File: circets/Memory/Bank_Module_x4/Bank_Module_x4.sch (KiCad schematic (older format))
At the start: 27 parts

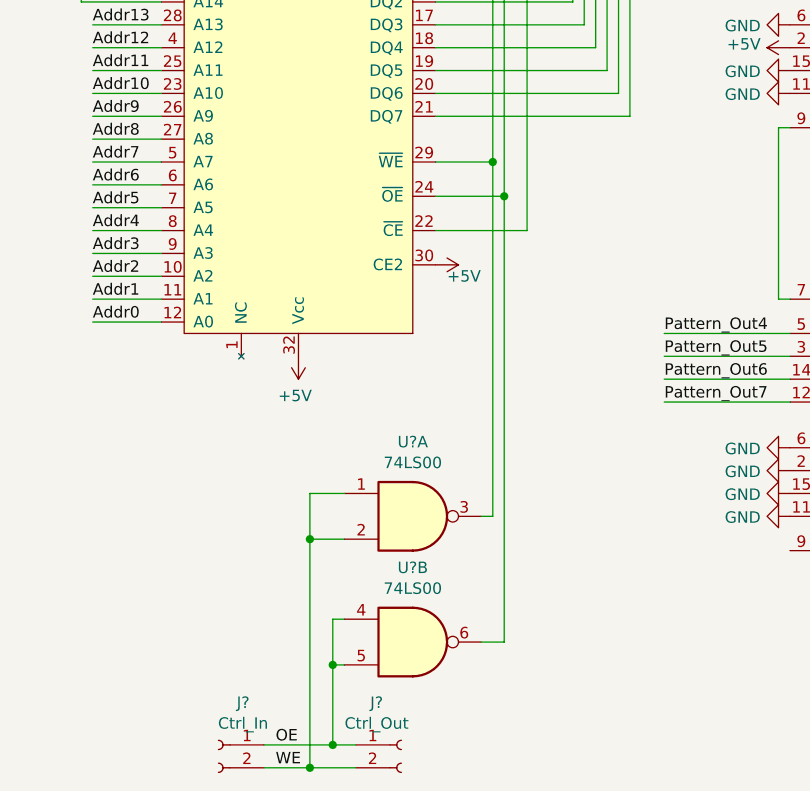
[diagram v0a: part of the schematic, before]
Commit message: Build Schematics for Bank Controller + minor optimaization to eliminat a NAND from Bank Modules
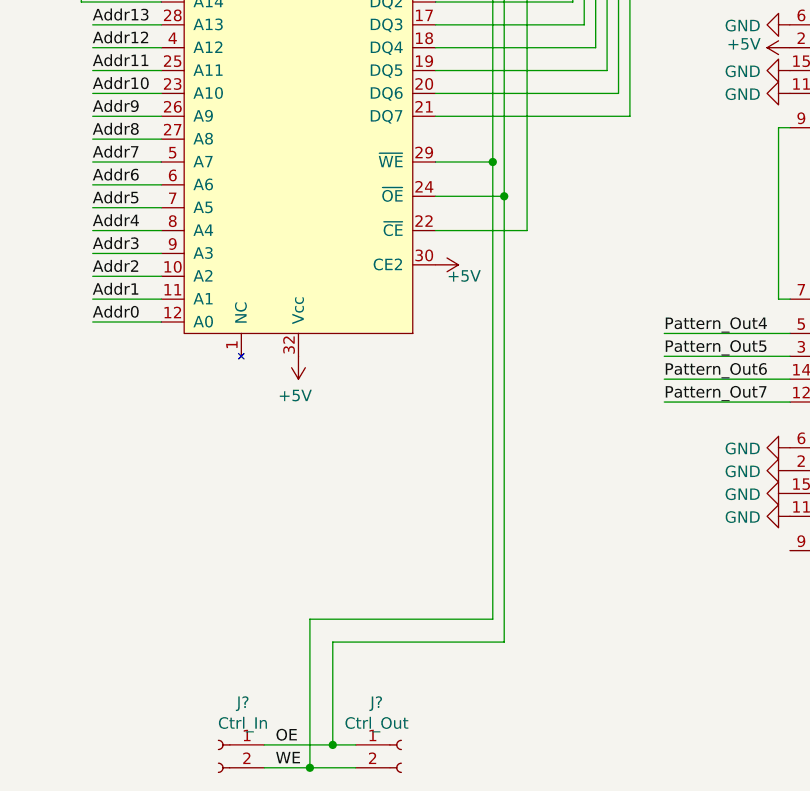
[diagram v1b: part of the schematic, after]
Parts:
- removed U? (x2): 74LS00, symbol 74xx:74LS00
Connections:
- net OE: now also U?.24 (~OE), U?.24 (~OE)
- net WE: now also U?.29 (~WE), U?.29 (~WE)
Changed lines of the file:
@@
 Comment1 ""
 Comment2 "https://github.com/jufo-ufo/Breadboard-Computer/blob/master/LICENSE"
-Comment3 "Apache License 2.0"
+Comment3 "License: Apache License 2.0"
 Comment4 "Author: Alexander Wersching"
 $EndDescr
@@
 	5300 6850 5600 6850
 Connection ~ 5600 6850
-Wire Wire Line
-	6350 6400 6250 6400
-Wire Wire Line
-	6300 5850 6250 5850
-Wire Wire Line
-	5650 5750 5500 5750
-Wire Wire Line
-	5650 6500 5600 6500
-Wire Wire Line
-	5600 6500 5600 6300
-Wire Wire Line
-	5600 6500 5600 6850
-Connection ~ 5600 6500
-Wire Wire Line
-	5500 5750 5500 5950
-Wire Wire Line
-	5500 5950 5500 6950
-Connection ~ 5500 5950
-Wire Wire Line
-	5650 5950 5500 5950
-Wire Wire Line
-	5600 6300 5650 6300
-$Comp
-L 74xx:74LS00 U?
-U 2 1 624E0AB4
-P 5950 6400
-F 0 "U?" H 5950 6725 50  0000 C CNN
-F 1 "74LS00" H 5950 6634 50  0000 C CNN
-F 2 "" H 5950 6400 50  0001 C CNN
-F 3 "http://www.ti.com/lit/gpn/sn74ls00" H 5950 6400 50  0001 C CNN
-	2    5950 6400
-	1    0    0    -1
-$EndComp
-$Comp
-L 74xx:74LS00 U?
-U 1 1 624DFB2D
-P 5950 5850
-F 0 "U?" H 5950 6175 50  0000 C CNN
-F 1 "74LS00" H 5950 6084 50  0000 C CNN
-F 2 "" H 5950 5850 50  0001 C CNN
-F 3 "http://www.ti.com/lit/gpn/sn74ls00" H 5950 5850 50  0001 C CNN
-	1    5950 5850
-	1    0    0    -1
-$EndComp
 $Comp
 L Computer_Component_Library:AS6C1008-55PCN U?
@@
 Connection ~ 6300 4300
 Wire Wire Line
-	6300 4300 6300 5850
+	6300 4300 6300 6300
 Wire Wire Line
 	6350 4450 6050 4450
@@
 Wire Wire Line
 	4250 1900 4150 1900
+Wire Wire Line
+	5600 6400 6350 6400
+Wire Wire Line
+	5600 6400 5600 6850
+Wire Wire Line
+	5500 6300 6300 6300
+Wire Wire Line
+	5500 6300 5500 6950
 $EndSCHEMATC

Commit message: Fixed alot of Issues in Memory Module
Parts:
- removed U?: 74LS86, symbol 74xx:74LS86
- removed U?: 74LS00, symbol 74xx:74LS00
- added U?: 74LS86, symbol 74xx:74LS86
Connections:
- net +5V: now also U?.15 (B3), U?.12; no longer U?.2 (B2)
- net GND: now also U?.2 (B2), U?.3; no longer U?.15 (B3)
- net OE: now also J?.2 (Pin_2), J?.2 (Pin_2); no longer J?.1 (Pin_1), J?.1 (Pin_1)
- net Pattern_In0: now also U?.5 (A1)
- net Pattern_In1: now also U?.3 (A2)
- net Pattern_In2: now also U?.14 (A3)
- net Pattern_In3: now also U?.12 (A4)
- net Pattern_In4: now also U?.5 (A1)
- net Pattern_In5: now also U?.3 (A2)
- net Pattern_In6: now also U?.14 (A3)
- net Pattern_In7: now also U?.12 (A4)
- net Pattern_Out0: no longer U?.5 (A1)
- net Pattern_Out1: no longer U?.3 (A2)
- net Pattern_Out2: no longer U?.14 (A3)
- net Pattern_Out3: no longer U?.12 (A4)
- net Pattern_Out4: no longer U?.5 (A1)
- net Pattern_Out5: no longer U?.3 (A2)
- net Pattern_Out6: no longer U?.14 (A3)
- net Pattern_Out7: no longer U?.12 (A4)
- net WE: now also J?.1 (Pin_1), J?.1 (Pin_1); no longer J?.2 (Pin_2), J?.2 (Pin_2)
- net at U?.22 (~CE), U?.22 (~CE): now also U?.11; no longer U?.13
- new net: U?.13, U?.13
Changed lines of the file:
@@
-$Comp
-L 74xx:74LS86 U?
-U 2 1 61EF8B7A
-P 2350 2850
-F 0 "U?" H 2350 3175 50  0000 C CNN
-F 1 "74LS86" H 2350 3084 50  0000 C CNN
-F 2 "" H 2350 2850 50  0001 C CNN
-F 3 "74xx/74ls86.pdf" H 2350 2850 50  0001 C CNN
-	2    2350 2850
-	1    0    0    -1
-$EndComp
 $Comp
 L 74xx:74LS86 U?
@@
 $EndComp
 Wire Wire Line
-	1500 2750 2050 2750
-Wire Wire Line
 	1450 3300 2050 3300
 Wire Wire Line
@@
 	1350 4400 2050 4400
 Wire Wire Line
-	1500 2300 1500 2750
-Wire Wire Line
 	1450 2400 1450 3300
 Wire Wire Line
@@
 Wire Wire Line
 	1850 3500 1850 1400
-Wire Wire Line
-	2050 2950 1900 2950
-Wire Wire Line
-	1900 2950 1900 1300
-Wire Wire Line
-	2650 2850 2800 2850
-Wire Wire Line
-	2800 2850 2800 1650
 Wire Wire Line
 	2850 1750 2850 3400
@@
 Wire Wire Line
 	3150 1750 2850 1750
-Wire Wire Line
-	2800 1650 3150 1650
 Wire Wire Line
 	3150 2250 3100 2250
@@
 	6050 1600 7000 1600
 $Comp
-L 74xx:74LS00 U?
-U 5 1 624E2056
-P 9500 1650
-F 0 "U?" H 9730 1696 50  0000 L CNN
-F 1 "74LS00" H 9730 1605 50  0000 L CNN
-F 2 "" H 9500 1650 50  0001 C CNN
-F 3 "http://www.ti.com/lit/gpn/sn74ls00" H 9500 1650 50  0001 C CNN
-	5    9500 1650
-	1    0    0    -1
-$EndComp
-$Comp
-L power:+5V #PWR?
-U 1 1 624EABED
-P 9500 1150
-F 0 "#PWR?" H 9500 1000 50  0001 C CNN
-F 1 "+5V" H 9515 1323 50  0000 C CNN
-F 2 "" H 9500 1150 50  0001 C CNN
-F 3 "" H 9500 1150 50  0001 C CNN
-	1    9500 1150
-	1    0    0    -1
-$EndComp
-$Comp
-L power:GND #PWR?
-U 1 1 624EB6EB
-P 9500 2150
-F 0 "#PWR?" H 9500 1900 50  0001 C CNN
-F 1 "GND" H 9505 1977 50  0000 C CNN
-F 2 "" H 9500 2150 50  0001 C CNN
-F 3 "" H 9500 2150 50  0001 C CNN
-	1    9500 2150
-	1    0    0    -1
-$EndComp
-Text Label 7050 3200 0    50   ~ 0
-Pattern_Out0
-Text Label 7050 3300 0    50   ~ 0
-Pattern_Out1
-Text Label 7050 3400 0    50   ~ 0
-Pattern_Out2
-Text Label 7050 3500 0    50   ~ 0
-Pattern_Out3
-Text Label 7050 5050 0    50   ~ 0
-Pattern_Out4
-Text Label 7050 5150 0    50   ~ 0
-Pattern_Out5
-Text Label 7050 5250 0    50   ~ 0
-Pattern_Out6
-Text Label 7050 5350 0    50   ~ 0
-Pattern_Out7
-$Comp
 L Computer_Component_Library:74HC283 U?
 U 1 1 6263D706
@@
 $EndComp
 Wire Wire Line
-	7050 5050 7600 5050
-Wire Wire Line
-	7600 5150 7050 5150
-Wire Wire Line
-	7050 5250 7600 5250
-Wire Wire Line
-	7600 5350 7050 5350
-Wire Wire Line
-	7050 3500 7600 3500
-Wire Wire Line
-	7050 3400 7600 3400
-Wire Wire Line
-	7600 3300 7050 3300
-Wire Wire Line
-	7050 3200 7600 3200
-Wire Wire Line
 	7600 4150 7550 4150
 Wire Wire Line
@@
 L power:+5V #PWR?
 U 1 1 62709DE4
-P 7600 3800
-F 0 "#PWR?" H 7600 3650 50  0001 C CNN
-F 1 "+5V" V 7615 3928 50  0000 L CNN
-F 2 "" H 7600 3800 50  0001 C CNN
-F 3 "" H 7600 3800 50  0001 C CNN
-	1    7600 3800
+P 7600 3900
+F 0 "#PWR?" H 7600 3750 50  0001 C CNN
+F 1 "+5V" V 7615 4028 50  0000 L CNN
+F 2 "" H 7600 3900 50  0001 C CNN
+F 3 "" H 7600 3900 50  0001 C CNN
+	1    7600 3900
 	0    -1   -1   0
 $EndComp
@@
 L power:GND #PWR?
 U 1 1 62717C3A
-P 7600 3900
-F 0 "#PWR?" H 7600 3650 50  0001 C CNN
-F 1 "GND" V 7605 3772 50  0000 R CNN
-F 2 "" H 7600 3900 50  0001 C CNN
-F 3 "" H 7600 3900 50  0001 C CNN
-	1    7600 3900
+P 7600 3800
+F 0 "#PWR?" H 7600 3550 50  0001 C CNN
+F 1 "GND" V 7605 3672 50  0000 R CNN
+F 2 "" H 7600 3800 50  0001 C CNN
+F 3 "" H 7600 3800 50  0001 C CNN
+	1    7600 3800
 	0    1    1    0
 $EndComp
@@
 Text Label 9200 3450 2    50   ~ 0
 Pattern_Out0
-Wire Wire Line
-	6450 650  6450 2300
 Connection ~ 6450 2300
 Wire Wire Line
@@
 Wire Wire Line
 	1850 1400 800  1400
-Wire Wire Line
-	1900 1300 800  1300
 $Comp
 L Connector:Conn_01x08_Female J?
@@
 Wire Wire Line
 	800  2400 1450 2400
-Wire Wire Line
-	800  2300 1500 2300
 $Comp
 L Connector:Conn_01x08_Female J?
@@
 Wire Wire Line
 	6050 3400 6550 3400
-Connection ~ 5500 6950
+Text Label 5350 6850 0    50   ~ 0
+WE
 Text Label 5350 6950 0    50   ~ 0
-WE
-Text Label 5350 6850 0    50   ~ 0
 OE
-Wire Wire Line
-	5500 6950 5300 6950
 $Comp
 L Connector:Conn_01x02_Female J?
@@
 	-1   0    0    -1
 $EndComp
-Wire Wire Line
-	5700 6950 5500 6950
 $Comp
 L Connector:Conn_01x02_Female J?
@@
 	1    0    0    -1
 $EndComp
-Wire Wire Line
-	5600 6850 5700 6850
-Wire Wire Line
-	5300 6850 5600 6850
-Connection ~ 5600 6850
 $Comp
 L Computer_Component_Library:AS6C1008-55PCN U?
@@
 	4450 1200 800  1200
 Connection ~ 4450 1200
-Wire Wire Line
-	1900 1300 4500 1300
-Connection ~ 1900 1300
 Connection ~ 4500 1300
 Wire Wire Line
-	6450 650  4250 650
-Wire Wire Line
-	4250 650  4250 1900
-Wire Wire Line
 	4250 1900 4150 1900
 Wire Wire Line
-	5600 6400 6350 6400
-Wire Wire Line
-	5600 6400 5600 6850
+	5550 6400 6350 6400
 Wire Wire Line
 	5500 6300 6300 6300
-Wire Wire Line
-	5500 6300 5500 6950
+Text Label 7550 3200 2    50   ~ 0
+Pattern_In0
+Text Label 7550 3300 2    50   ~ 0
+Pattern_In1
+Text Label 7550 3400 2    50   ~ 0
+Pattern_In2
+Text Label 7550 3500 2    50   ~ 0
+Pattern_In3
+Text Label 7550 5050 2    50   ~ 0
+Pattern_In4
+Text Label 7550 5150 2    50   ~ 0
+Pattern_In5
+Text Label 7550 5250 2    50   ~ 0
+Pattern_In6
+Text Label 7550 5350 2    50   ~ 0
+Pattern_In7
+Wire Wire Line
+	7550 3200 7600 3200
+Wire Wire Line
+	7600 3300 7550 3300
+Wire Wire Line
+	7550 3400 7600 3400
+Wire Wire Line
+	7600 3500 7550 3500
+Wire Wire Line
+	7550 5050 7600 5050
+Wire Wire Line
+	7600 5150 7550 5150
+Wire Wire Line
+	7550 5250 7600 5250
+Wire Wire Line
+	7600 5350 7550 5350
+$Comp
+L 74xx:74LS86 U?
+U 4 1 645ED5B6
+P 4700 700
+F 0 "U?" H 4850 850 50  0000 C CNN
+F 1 "74LS86" H 4700 500 50  0000 C CNN
+F 2 "" H 4700 700 50  0001 C CNN
+F 3 "74xx/74ls86.pdf" H 4700 700 50  0001 C CNN
+	4    4700 700
+	1    0    0    -1
+$EndComp
+Wire Wire Line
+	5000 700  6450 700
+Wire Wire Line
+	6450 700  6450 2300
+Wire Wire Line
+	4250 800  4250 1900
+Wire Wire Line
+	4400 800  4250 800
+$Comp
+L power:+5V #PWR?
+U 1 1 6461B693
+P 4400 600
+F 0 "#PWR?" H 4400 450 50  0001 C CNN
+F 1 "+5V" V 4415 728 50  0000 L CNN
+F 2 "" H 4400 600 50  0001 C CNN
+F 3 "" H 4400 600 50  0001 C CNN
+	1    4400 600
+	0    -1   -1   0
+$EndComp
+Wire Wire Line
+	5300 6850 5500 6850
+Wire Wire Line
+	5300 6950 5550 6950
+Wire Wire Line
+	5500 6300 5500 6850
+Connection ~ 5500 6850
+Wire Wire Line
+	5500 6850 5700 6850
+Connection ~ 5550 6950
+Wire Wire Line
+	5550 6950 5700 6950
+Wire Wire Line
+	5550 6400 5550 6950
+Wire Wire Line
+	800  1300 4500 1300
+$Comp
+L power:GND #PWR?
+U 1 1 64669F14
+P 3150 1650
+F 0 "#PWR?" H 3150 1400 50  0001 C CNN
+F 1 "GND" V 3155 1522 50  0000 R CNN
+F 2 "" H 3150 1650 50  0001 C CNN
+F 3 "" H 3150 1650 50  0001 C CNN
+	1    3150 1650
+	0    1    1    0
+$EndComp
 $EndSCHEMATC
